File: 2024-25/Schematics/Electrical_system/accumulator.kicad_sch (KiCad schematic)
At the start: 17 parts, among them K1 GV24 1BAX, K3 P115 BDA, K4 GV24 1BAX, U3 RSB, U5 Volt_indic

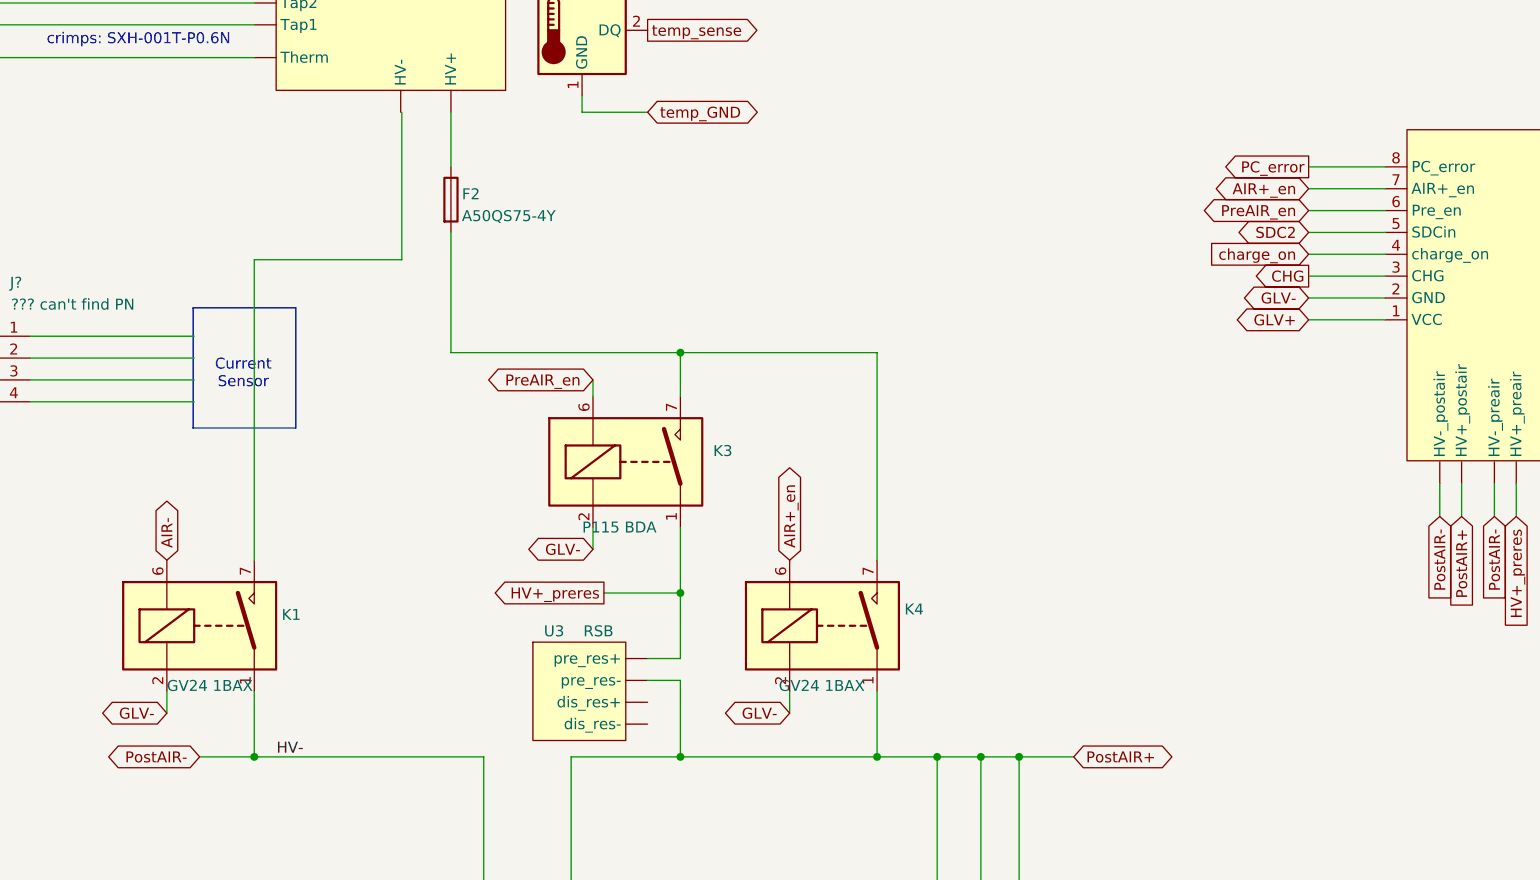
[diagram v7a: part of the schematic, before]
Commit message: added inline voltage divider and fixed relay wiring
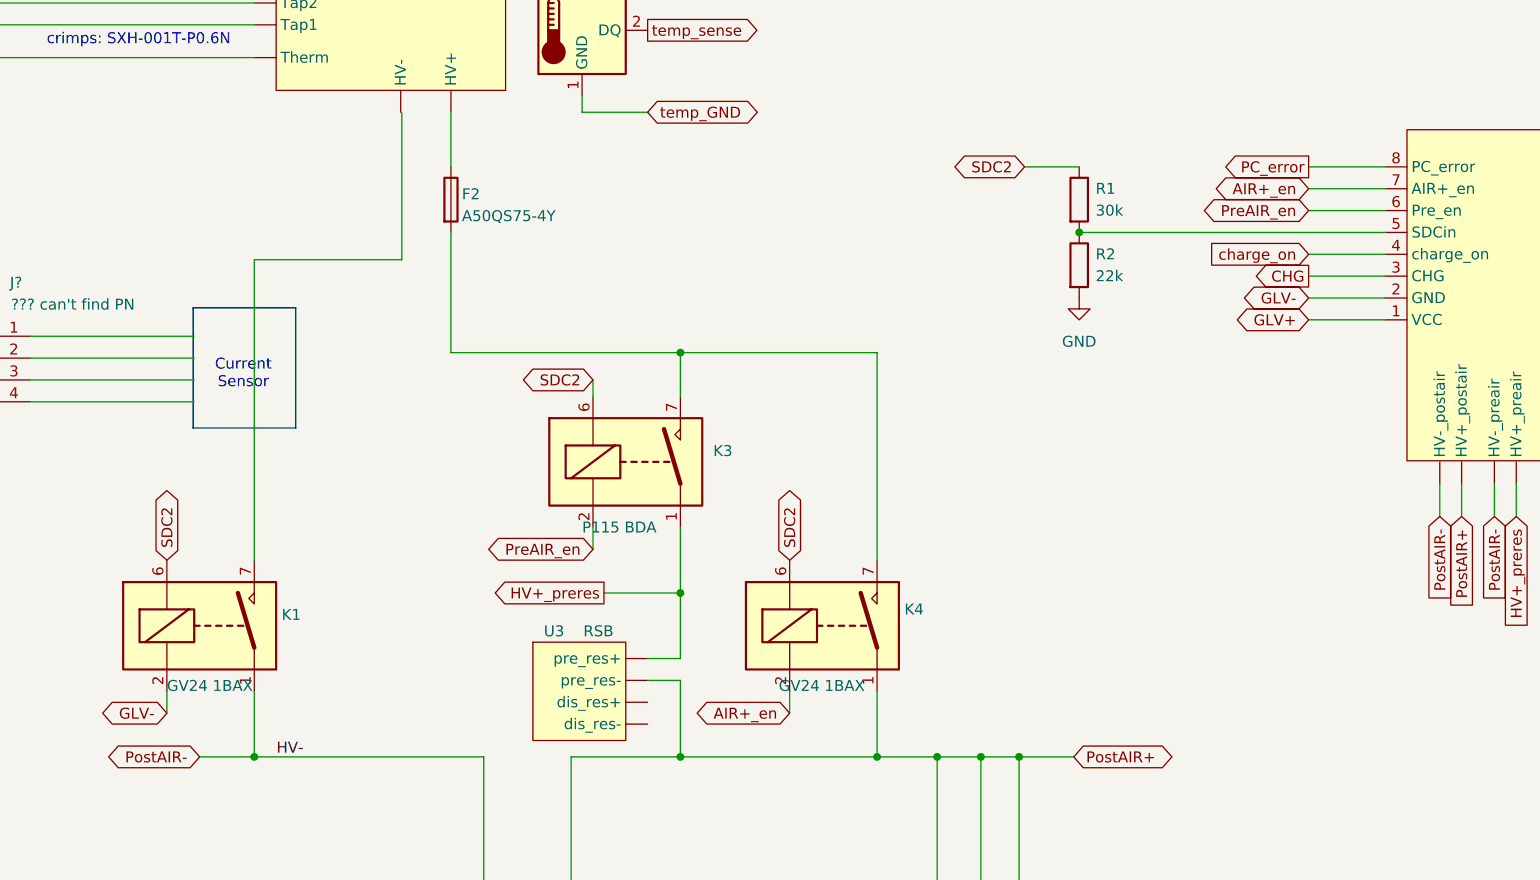
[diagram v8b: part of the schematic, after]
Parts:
- added R1: 30k, symbol Device:R
- added R2: 22k, symbol Device:R
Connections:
- net AIR- is gone; now on net SDC2: K1.6
- net AIR+_en: now also K4.2; no longer K4.6
- net GNDPWR: no longer K3.2, K4.2
- net PreAIR_en: now also K3.2; no longer K3.6
- net SDC2: now also K3.6, K4.6, R1.1; no longer U?.5 (SDCin)
- net at U?. (Tap3): no longer U?. (GND_Lug)
- new net: R1.2, R2.1, U?.5 (SDCin)
- new net: U?. (GND_Lug), U?. (Tap3) (x4)
- new net GND: R2.2
- now unconnected: U?. (Tap3), U?. (Tap3), U?. (Tap3)
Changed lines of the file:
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@@
 	)
 	(junction
+		(at 297.815 104.14)
+		(diameter 0)
+		(color 0 0 0 0)
+	)
+	(junction
 		(at 251.46 165.1)
 		(diameter 0)
@@
 	(wire
 		(pts
-			(xy 324.485 104.14) (xy 333.375 104.14)
-		)
-		(stroke
-			(width 0)
-			(type default)
-		)
-	)
-	(wire
-		(pts
 			(xy 96.52 57.15) (xy 101.6 57.15)
 		)
@@
 		)
 	)
+	(wire
+		(pts
+			(xy 291.465 96.52) (xy 297.815 96.52)
+		)
+		(stroke
+			(width 0)
+			(type default)
+		)
+	)
 	(bus
 		(pts
@@
 		)
 	)
+	(wire
+		(pts
+			(xy 297.815 104.14) (xy 333.375 104.14)
+		)
+		(stroke
+			(width 0)
+			(type default)
+		)
+	)
 	(bus
 		(pts
@@
 		)
 	)
+	(global_label "SDC2"
+		(shape bidirectional)
+		(at 291.465 96.52 180)
+		(fields_autoplaced yes)
+		(effects
+			(font
+				(size 1.27 1.27)
+			)
+			(justify right)
+		)
+		(property "Intersheetrefs" "${INTERSHEET_REFS}"
+			(at 282.4095 96.52 0)
+			(effects
+				(font
+					(size 1.27 1.27)
+				)
+				(justify right)
+				(hide yes)
+			)
+		)
+	)
 	(global_label "charge_on"
 		(shape input)
@@
 		)
 	)
-	(global_label "SDC2"
-		(shape bidirectional)
-		(at 324.485 104.14 180)
-		(fields_autoplaced yes)
-		(effects
-			(font
-				(size 1.27 1.27)
-			)
-			(justify right)
-		)
-		(property "Intersheetrefs" "${INTERSHEET_REFS}"
-			(at 315.4295 104.14 0)
-			(effects
-				(font
-					(size 1.27 1.27)
-				)
-				(justify right)
-				(hide yes)
-			)
-		)
-	)
 	(global_label "PostAIR+"
 		(shape input)
@@
 		)
 	)
-	(global_label "AIR-"
+	(global_label "SDC2"
 		(shape bidirectional)
 		(at 191.77 142.24 90)
@@
 		)
 		(property "Intersheetrefs" "${INTERSHEET_REFS}"
-			(at 191.77 133.6871 90)
+			(at 191.77 133.1845 90)
 			(effects
 				(font
@@
 		)
 	)
-	(global_label "AIR+_en"
+	(global_label "SDC2"
 		(shape bidirectional)
 		(at 264.16 142.24 90)
@@
 		)
 		(property "Intersheetrefs" "${INTERSHEET_REFS}"
-			(at 264.16 130.4025 90)
+			(at 264.16 133.1845 90)
 			(effects
 				(font
@@
 		)
 	)
-	(global_label "GLV-"
+	(global_label "AIR+_en"
 		(shape bidirectional)
 		(at 264.16 160.02 180)
@@
 		)
 		(property "Intersheetrefs" "${INTERSHEET_REFS}"
-			(at 255.1838 160.02 0)
+			(at 252.3225 160.02 0)
 			(effects
 				(font
@@
 		)
 	)
-	(global_label "PreAIR_en"
+	(global_label "SDC2"
 		(shape bidirectional)
 		(at 241.3 121.285 180)
@@
 		)
 		(property "Intersheetrefs" "${INTERSHEET_REFS}"
-			(at 227.8901 121.285 0)
+			(at 232.2445 121.285 0)
 			(effects
 				(font
@@
 		)
 	)
-	(global_label "GLV-"
+	(global_label "PreAIR_en"
 		(shape bidirectional)
 		(at 241.3 140.97 180)
@@
 		)
 		(property "Intersheetrefs" "${INTERSHEET_REFS}"
-			(at 232.3238 140.97 0)
+			(at 227.8901 140.97 0)
 			(effects
 				(font
@@
 	)
 	(symbol
+		(lib_id "Device:R")
+		(at 297.815 107.95 0)
+		(unit 1)
+		(exclude_from_sim no)
+		(in_bom yes)
+		(on_board yes)
+		(dnp no)
+		(fields_autoplaced yes)
+		(property "Reference" "R2"
+			(at 299.72 106.6799 0)
+			(effects
+				(font
+					(size 1.27 1.27)
+				)
+				(justify left)
+			)
+		)
+		(property "Value" "22k"
+			(at 299.72 109.2199 0)
+			(effects
+				(font
+					(size 1.27 1.27)
+				)
+				(justify left)
+			)
+		)
+		(property "Footprint" ""
+			(at 296.037 107.95 90)
+			(effects
+				(font
+					(size 1.27 1.27)
+				)
+				(hide yes)
+			)
+		)
+		(property "Datasheet" "~"
+			(at 297.815 107.95 0)
+			(effects
+				(font
+					(size 1.27 1.27)
+				)
+				(hide yes)
+			)
+		)
+		(property "Description" "Resistor"
+			(at 297.815 107.95 0)
+			(effects
+				(font
+					(size 1.27 1.27)
+				)
+				(hide yes)
+			)
+		)
+		(pin "1"
+		)
+		(pin "2"
+		)
+		(instances
+			(project "accumulator"
+				(path "/257053c5-9a9c-4e07-83c1-3de2ea3e3dc0"
+					(reference "R2")
+					(unit 1)
+				)
+			)
+		)
+	)
+	(symbol
 		(lib_id "Random:RSB")
 		(at 241.3 157.48 0)
@@
 					(unit 1)
 				)
+			)
+		)
+	)
+	(symbol
+		(lib_id "Device:R")
+		(at 297.815 100.33 0)
+		(unit 1)
+		(exclude_from_sim no)
+		(in_bom yes)
+		(on_board yes)
+		(dnp no)
+		(fields_autoplaced yes)
+		(property "Reference" "R1"
+			(at 299.72 99.0599 0)
+			(effects
+				(font
+					(size 1.27 1.27)
+				)
+				(justify left)
+			)
+		)
+		(property "Value" "30k"
+			(at 299.72 101.5999 0)
+			(effects
+				(font
+					(size 1.27 1.27)
+				)
+				(justify left)
+			)
+		)
+		(property "Footprint" ""
+			(at 296.037 100.33 90)
+			(effects
+				(font
+					(size 1.27 1.27)
+				)
+				(hide yes)
+			)
+		)
+		(property "Datasheet" "~"
+			(at 297.815 100.33 0)
+			(effects
+				(font
+					(size 1.27 1.27)
+				)
+				(hide yes)
+			)
+		)
+		(property "Description" "Resistor"
+			(at 297.815 100.33 0)
+			(effects
+				(font
+					(size 1.27 1.27)
+				)
+				(hide yes)
+			)
+		)
+		(pin "1"
+		)
+		(pin "2"
+		)
+		(instances
+			(project "accumulator"
+				(path "/257053c5-9a9c-4e07-83c1-3de2ea3e3dc0"
+					(reference "R1")
+					(unit 1)
+				)
+			)
+		)
+	)
+	(symbol
+		(lib_id "power:GND")
+		(at 297.815 111.76 0)
+		(unit 1)
+		(exclude_from_sim no)
+		(in_bom yes)
+		(on_board yes)
+		(dnp no)
+		(fields_autoplaced yes)
+		(property "Reference" "#PWR01"
+			(at 297.815 118.11 0)
+			(effects
+				(font
+					(size 1.27 1.27)
+				)
+				(hide yes)
+			)
+		)
+		(property "Value" "GND"
+			(at 297.815 116.84 0)
+			(effects
+				(font
+					(size 1.27 1.27)
+				)
+			)
+		)
+		(property "Footprint" ""
+			(at 297.815 111.76 0)
+			(effects
+				(font
+					(size 1.27 1.27)
+				)
+				(hide yes)
+			)
+		)
+		(property "Datasheet" ""
+			(at 297.815 111.76 0)
+			(effects
+				(font
+					(size 1.27 1.27)
+				)
+				(hide yes)
+			)
+		)
+		(property "Description" "Power symbol creates a global label with name \"GND\" , ground"
+			(at 297.815 111.76 0)
+			(effects
+				(font
+					(size 1.27 1.27)
+				)
+				(hide yes)
+			)
+		)
+		(pin "1"
+		)
+		(instances
+			(project "accumulator"
+				(path "/257053c5-9a9c-4e07-83c1-3de2ea3e3dc0"
+					(reference "#PWR01")
+					(unit 1)
+				)
